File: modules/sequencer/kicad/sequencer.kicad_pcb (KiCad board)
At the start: 2 copper layers, 152.2 x 104.5 mm, 127 parts, among them P1 CONN_01X03, P2 CONN_02X03, P3 CONN_01X03, P4 CONN_02X03, P5 CONN_02X03, P6 CONN_01X02, Q1 MMBT3904, Q10 MMBT3906, Q2 MMBT3906, Q3 MMBT3906, Q4 MMBT3906, Q5 MMBT3906, Q6 MMBT3906, Q7 MMBT3906, Q8 MMBT3906, Q9 MMBT3906, SW1 SW_PUSH_SMALL_H, SW10 SW_PUSH_SMALL_H, SW11 LED-BUTTON, SW12 SWITCH_INV_MSM, SW13 SW_PUSH_DPDT, SW14 SW_PUSH_DPDT, SW15 SW_PUSH_DPDT, SW16 SW_PUSH_DPDT, SW17 SW_PUSH_DPDT, SW18 SW_PUSH_DPDT, SW19 Switch_SPDT_x2, SW2 SW_PUSH_SMALL_H, SW20 SW_PUSH_DPDT, SW21 SW_PUSH_DPDT, SW3 SW_PUSH_SMALL_H, SW4 SW_PUSH_SMALL_H, SW5 SW_PUSH_SMALL_H, SW6 SW_PUSH_SMALL_H, SW7 SW_PUSH_SMALL_H, SW8 SW_PUSH_SMALL_H, SW9 SW_PUSH_SMALL_H, U1 MAX7221, U10 MCP3202, U11 MC14551B, U2 MCP23S17, U3 ATmega32U4-AU(edit), U4 MCP4921-E/SN, U5 74LS138, U6 CD4051, U7 CD4051, U8 TL074, U9 TS12A4517, X1 CRYSTAL_SMD2

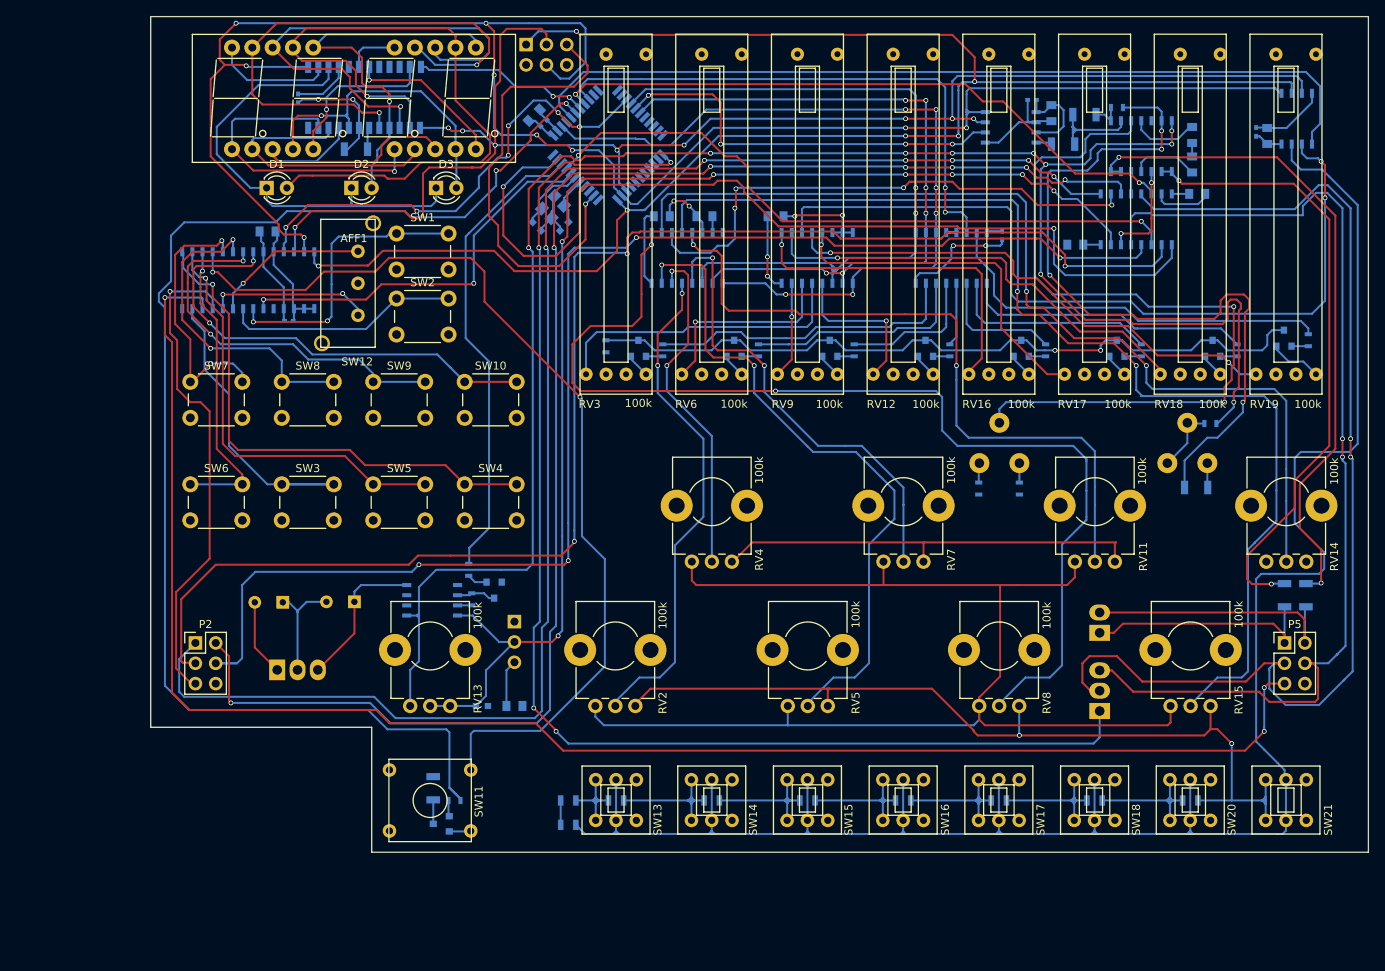
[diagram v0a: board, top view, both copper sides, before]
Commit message: Add screw holes to seq. PCB, finish panel alignment
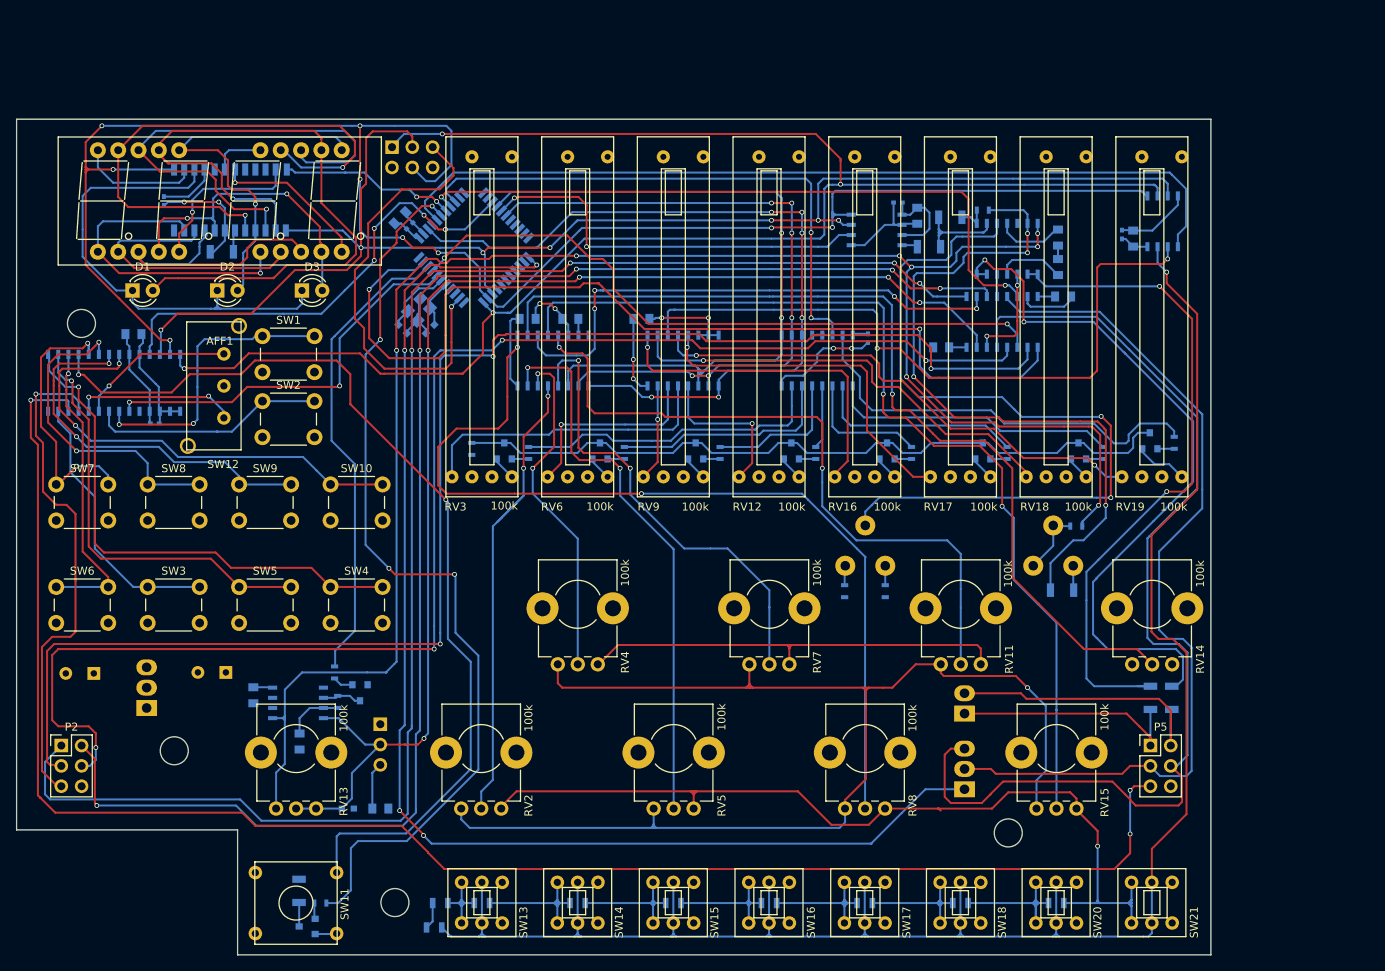
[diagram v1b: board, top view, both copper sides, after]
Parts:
- added C24: 10u, Capacitors_SMD:C_0805, B.Cu at (106.4, 111.2)
- added C25: 10u, Capacitors_SMD:C_0805, B.Cu at (112.2, 117.0)
- moved C4 25.2 mm to (86.5, 108.5)
- moved R11 21.1 mm to (180.3, 98.2)
- moved R20 21.1 mm to (209.3, 90.0)
- moved R29 21.1 mm to (133.7, 80.4)
- moved R6 21.1 mm to (185.4, 98.2)
- moved SW4 21.1 mm to (116.1, 97.6)
- moved SW5 21.1 mm to (104.6, 97.6)
- moved SW6 21.1 mm to (81.8, 97.6)
- moved C11 21.1 mm to (154.9, 64.1)
- moved C16 21.1 mm to (189.4, 51.2)
- moved C19 21.1 mm to (183.3, 66.5)
- moved C7 21.1 mm to (192.4, 67.7)
- moved R7 21.1 mm to (190.9, 55.1)
- moved R9 21.1 mm to (193.5, 51.4)
- moved U1 21.1 mm to (103.5, 49.3)
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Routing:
- net RUN_INDICATOR: track 166.4 -> 115.7 mm, vias 2 -> 4
- net GATE_OUT: track 138.4 -> 110.9 mm, vias 2 -> 0
- net Net-(RV15-Pad2): track 142.0 -> 122.4 mm
- net Net-(RV8-Pad2): track 133.8 -> 114.8 mm
- net Net-(U10-Pad2): track 102.4 -> 86.9 mm
- net VCC: track 281.1 -> 265.6 mm, vias 8 -> 7
- net Net-(RV5-Pad2): track 84.0 -> 70.6 mm
- net GND: track 93.8 -> 80.4 mm
- net Net-(R30-Pad1): track 253.9 -> 240.6 mm, vias 0 -> 1
- net CHAIN_TRIGGER: track 170.9 -> 180.0 mm
- net Net-(R20-Pad1): track 228.7 -> 221.0 mm, vias 10 -> 8
- net Net-(R31-Pad2): track 77.8 -> 85.1 mm
- net Net-(R16-Pad1): track 95.7 -> 88.7 mm
- net Net-(R32-Pad2): track 84.3 -> 89.7 mm
- net Net-(RV14-Pad2): track 122.0 -> 116.9 mm, vias 2 -> 1
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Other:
- board size 152.2 x 104.5 mm -> 149.3 x 104.5 mm
- board text removed: "TODO: decoupling caps for this analog switch"

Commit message: Finish routing nets on sequencer PCB
TODO: silkscreen
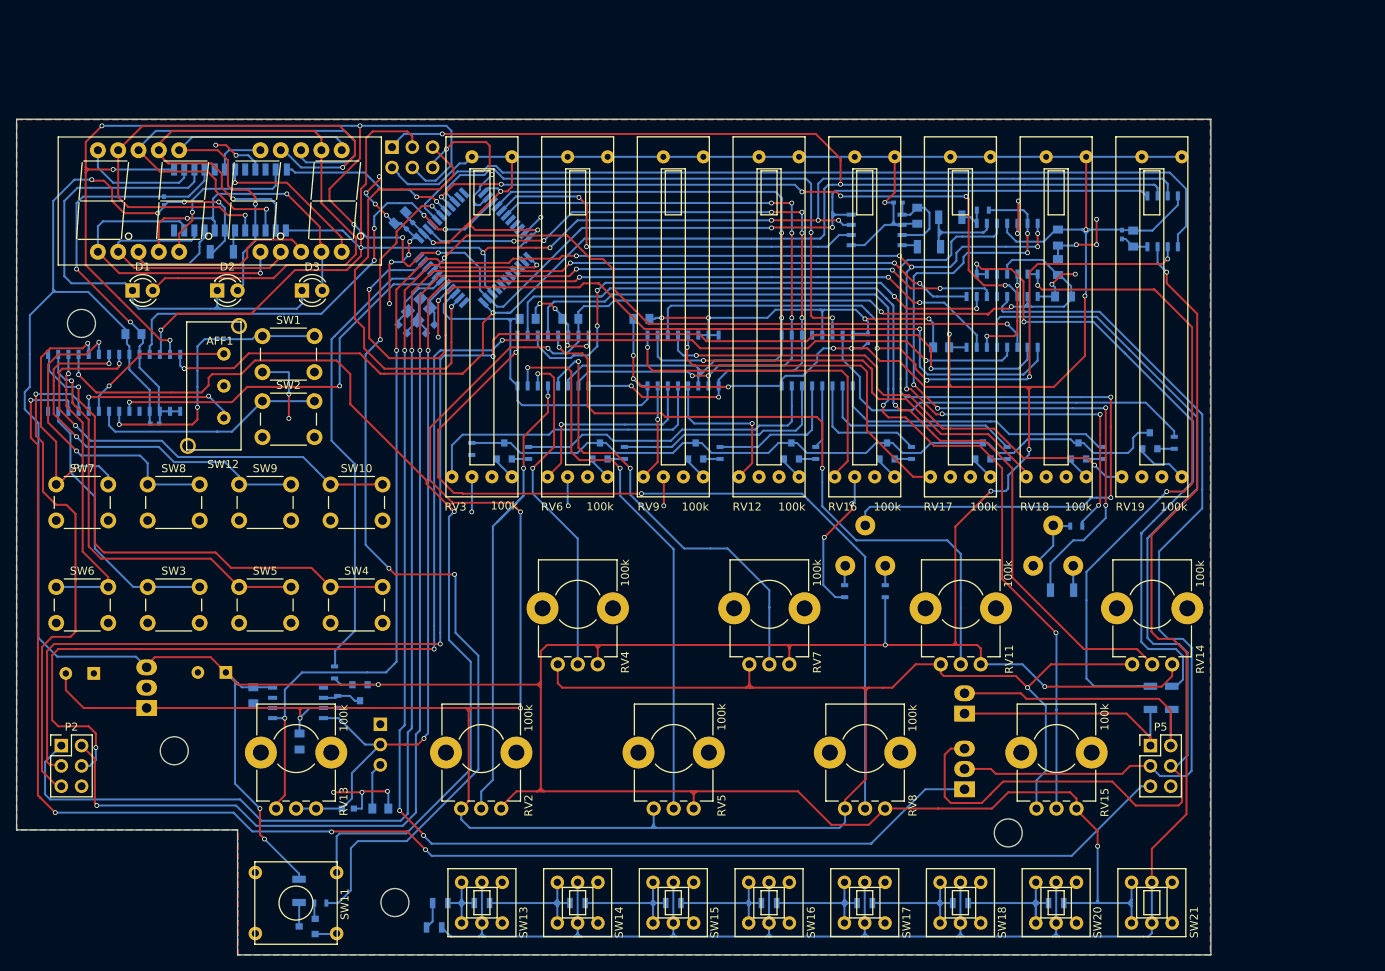
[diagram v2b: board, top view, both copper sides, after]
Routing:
- net VCC: track 265.6 -> 834.6 mm, vias 7 -> 24
- net VEE: track 182.6 -> 405.9 mm, vias 1 -> 7
- net GND: track 80.4 -> 282.5 mm, vias 4 -> 42
- net Net-(R32-Pad2): track 89.7 -> 81.8 mm
- net SPI_MOSI: track 230.7 -> 237.2 mm
- net CHAIN_OUT: track 207.7 -> 201.7 mm, vias 3 -> 4
- net Net-(D1-Pad1): track 60.0 -> 65.6 mm
- net Net-(RV8-Pad2): track 114.8 -> 111.2 mm
- net Net-(RV1-Pad2): track 101.1 -> 104.3 mm
- net GATE_OUT: track 110.9 -> 113.7 mm
- net DECODER_ENABLE: track 69.8 -> 72.4 mm
- net Net-(R20-Pad1): track 221.0 -> 223.4 mm, vias 8 -> 11
- net Net-(R16-Pad1): track 88.7 -> 91.0 mm, vias 4 -> 6
- net Net-(RV15-Pad2): track 122.4 -> 124.2 mm
- net CV2: track 67.1 -> 68.8 mm
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- added copper zone on B.Cu, net GND
- added copper zone on F.Cu, net GND

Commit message: Add test points, finish silkscreen on sequencer board
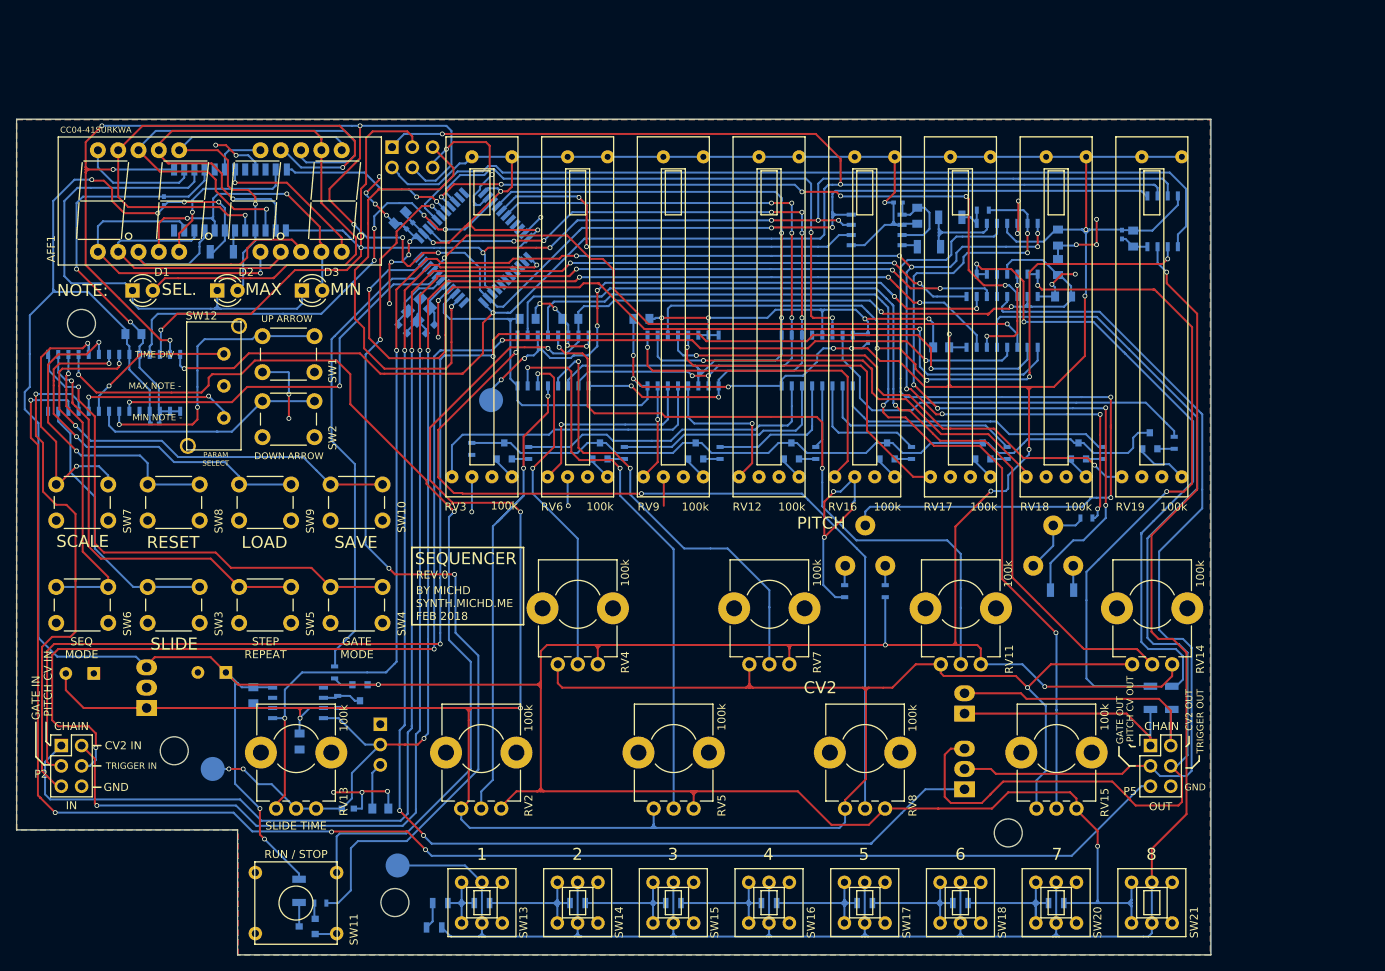
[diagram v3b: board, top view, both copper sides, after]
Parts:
- added W1: CV2, Measurement_Points:Measurement_Point_Round-SMD-Pad_Big, B.Cu at (136.1, 74.3)
- added W2: PITCH_CV, Measurement_Points:Measurement_Point_Round-SMD-Pad_Big, B.Cu at (101.3, 120.4)
- added W3: STEP_SELECT, Measurement_Points:Measurement_Point_Round-SMD-Pad_Big, B.Cu at (124.5, 132.5)
- R13, R19, R23, R25, R28, R4, R5, R8: value 1k -> 1k, .1%
- U3: value ATmega32U4-AU(edit) -> ATmega32U4
- U4: value MCP4921-E/SN -> MCP4921
- moved R20 1.63 mm to (210.6, 89.0)
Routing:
- net PITCH_CV: track 159.3 -> 171.8 mm, vias 5 -> 7
- net CV2: track 68.8 -> 80.3 mm, vias 4 -> 6
- net Net-(R30-Pad1): track 240.6 -> 252.0 mm
- net GND: track 282.5 -> 292.2 mm, vias 42 -> 41
- net Net-(R20-Pad2): track 8.24 -> 10.2 mm
- net Net-(R20-Pad1): track 223.4 -> 221.9 mm
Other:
- board text added: "+5V"
- board text added: "-5V"
- board text added: "1"
- board text added: "12-BIT PITCH CV DAC"
- board text added: "2"
- board text added: "3"
- board text added: "4"
- board text added: "4x ANALOG SPDT SW SWITCHING BETWEEN LOCAL AND CHAIN SIGNALS"
- board text added: "5"
- board text added: "6"
- board text added: "7"
- board text added: "8"
- board text added: "ANALOG SW SLIDE ON/OFF"
- board text added: "BY MICHD FEB 2018"
- board text added: "BY MICHD SYNTH.MICHD.ME FEB 2018"
- board text added: "CHAIN"
- board text added: "CRYSTAL"
- board text added: "CV2"
- board text added: "CV2 IN"
- board text added: "CV2 MUX"
- board text added: "CV2 OUT"
- board text added: "DECODER FOR LEDS"
- board text added: "DISPLAY DRIVER"
- board text added: "DOWN"
- board text added: "DOWN ARROW"
- board text added: "DUAL 12-BIT ADC PITCH CV IN, STEP SELECT"
- board text added: "EXT CLK IN"
- board text added: "GATE IN"
- board text added: "GATE MODE"
- board text added: "GATE OUT"
- board text added: "GND"
- board text added: "GPIO PORT EXPANDER (BUTTONS)"
- board text added: "IN"
- board text added: "ISP PROGRAMMING"
- board text added: "LOAD"
- board text added: "LONGER SLIDE TIME"
- board text added: "MAX"
- board text added: "MAX NOTE -"
- board text added: "MICRO CONTROLLER"
- board text added: "MIN"
- board text added: "MIN NOTE -"
- board text added: "NOTE:"
- board text added: "OUT"
- board text added: "PARAM SELECT"
- board text added: "PITCH"
- board text added: "PITCH AMP"
- board text added: "PITCH CV DC OFFSET"
- board text added: "PITCH CV IN"
- board text added: "PITCH CV MUX"
- board text added: "PITCH CV OUT"
- board text added: "POWER"
- board text added: "QUAD OPAMP SCALING, BUFFERING"
- board text added: "RESET"
- board text added: "REV.0"
- board text added: "RUN / STOP"
- board text added: "SAVE"
- board text added: "SCALE"
- board text added: "SEL."
- board text added: "SEQ MODE"
- board text added: "SEQUENCER"
- board text added: "SLIDE"
- board text added: "SLIDE TIME"
- board text added: "STEP REPEAT"
- board text added: "TIME DIV -"
- board text added: "TRIGGER IN"
- board text added: "TRIGGER OUT"
- board text added: "UP"
- board text added: "UP ARROW"

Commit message: Finish sequencer PCB (and sent off for fab at this point)
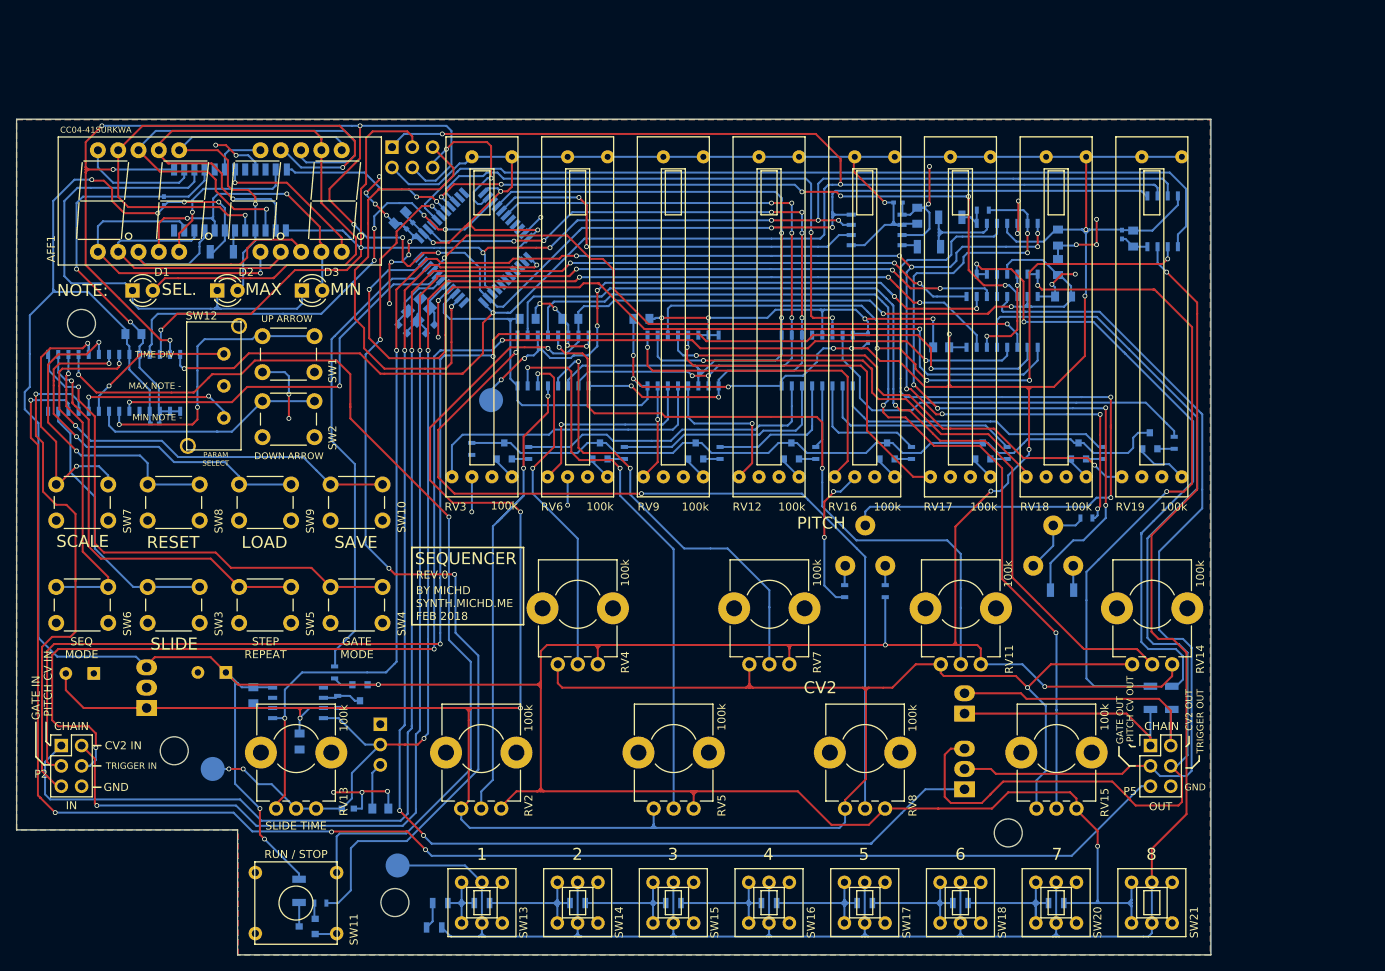
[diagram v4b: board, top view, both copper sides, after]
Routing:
- net GND: track 292.2 -> 285.8 mm, vias 41 -> 43
- net Net-(SW11-Pad1): track 121.3 -> 120.1 mm
- net VCC: track 834.6 -> 835.3 mm
- net Net-(U10-Pad2): track 87.6 -> 88.2 mm
